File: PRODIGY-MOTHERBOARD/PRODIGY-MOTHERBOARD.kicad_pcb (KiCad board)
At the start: 2 copper layers, 165 x 125 mm, 285 parts, among them J10 RTD_PT100, J11 Can, J12 USB_A, J13 SPI_OUT, J14 MOTOR, J15 12V OUT, J16 Neopixel, J17 SERIAL, J18 I2C, J19 KEYPAD_MATRIX, J2 USB_C_Receptacle, J20 OLED, J21 DM3BT-DSF-PEJS/C, J3 Conn_02x20_Odd_Even, J5 Barrel_Jack_MountingPin, J6 USB_C_Receptacle, J9 A_IN, Q1 BC850, Q2 BC850, Q3 BS870, Q4 BC850, Q5 ALS-PDIC15-21B/TR8, SW1 SW_Push, SW2 SW_Push, SW3 SW_Push, SW4 SW_Push, SW5 SW_Push, SW6 SW_Push, U1 RT9742AGJ5F, U10 PCF8574, U11 HDC1080, U12 LIS2DH12TR, U13 TXS0108EPW, U15 CC56-12YWA, U16 PN5321A3HN_C1xx, U17 CR2013-MI2120, U18 SN74LVC1T45DBV, U19 TSDP341xx, U2 TPS54331DR, U20 TSDP341xx, U21 MCP6021RT-E/OT, U22 LMP2011, U23 LM4125AIM5-2.5, U24 LMP2011, U25 LMP2011, U26 LMP2011, U27 IP4252CZ16, U28 RT9742AGJ5F, U3 TPS54331DR, U4 TJA1051T-E, U5 DRV8870DDA, U6 PCA9306DC, U7 PCA9306DC, U8 SN74LVC1T45DBV, U9 PCF8574

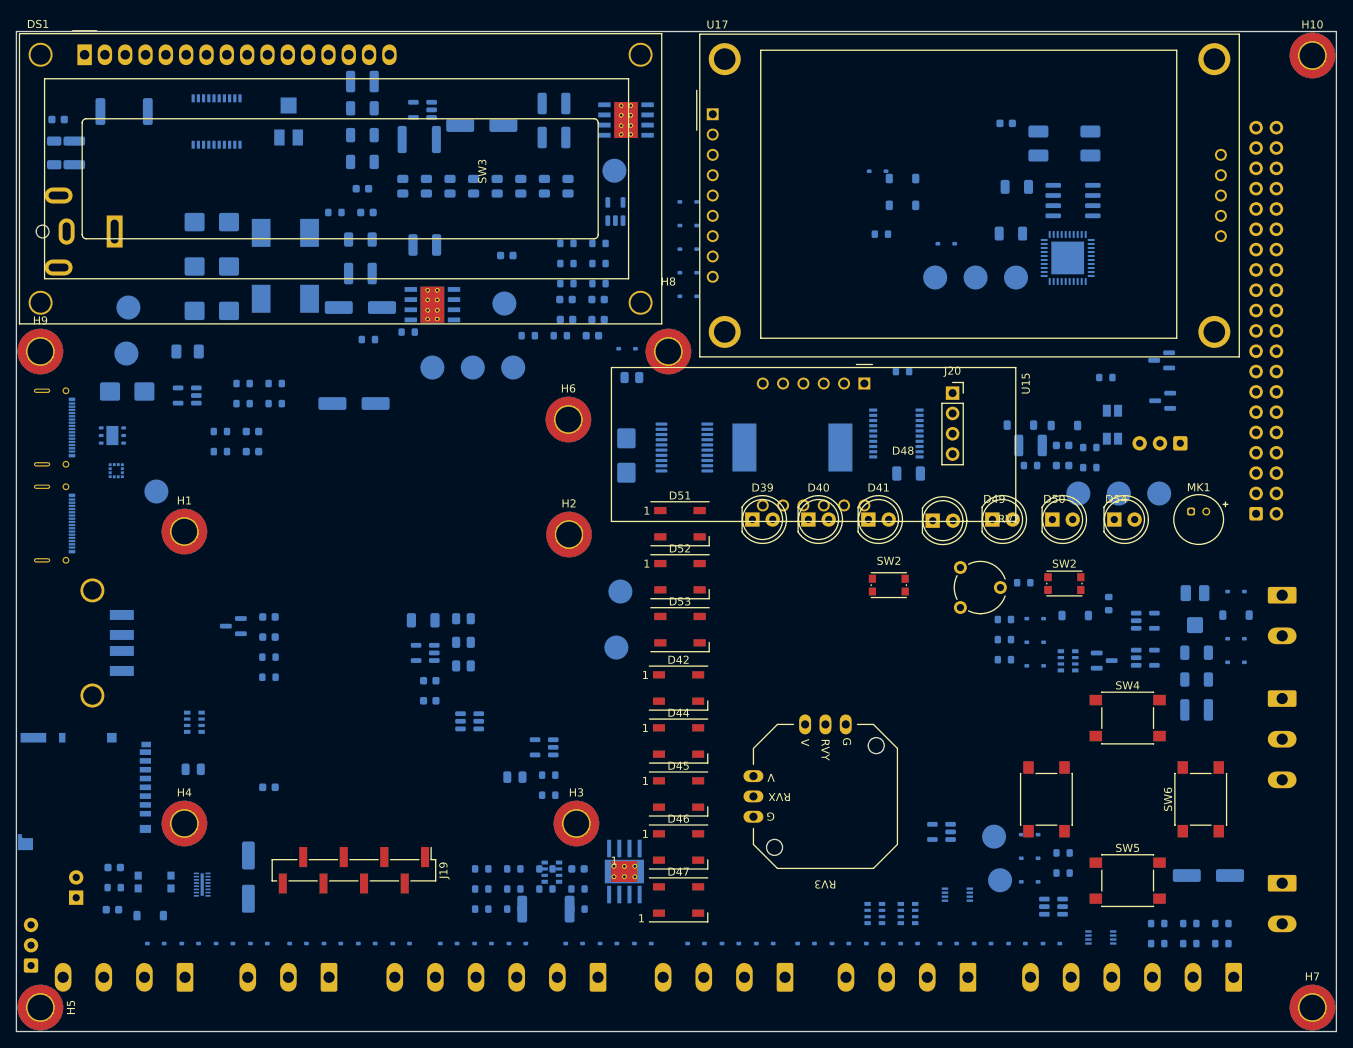
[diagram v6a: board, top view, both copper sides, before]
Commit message: changed breakout connectors and bpc size
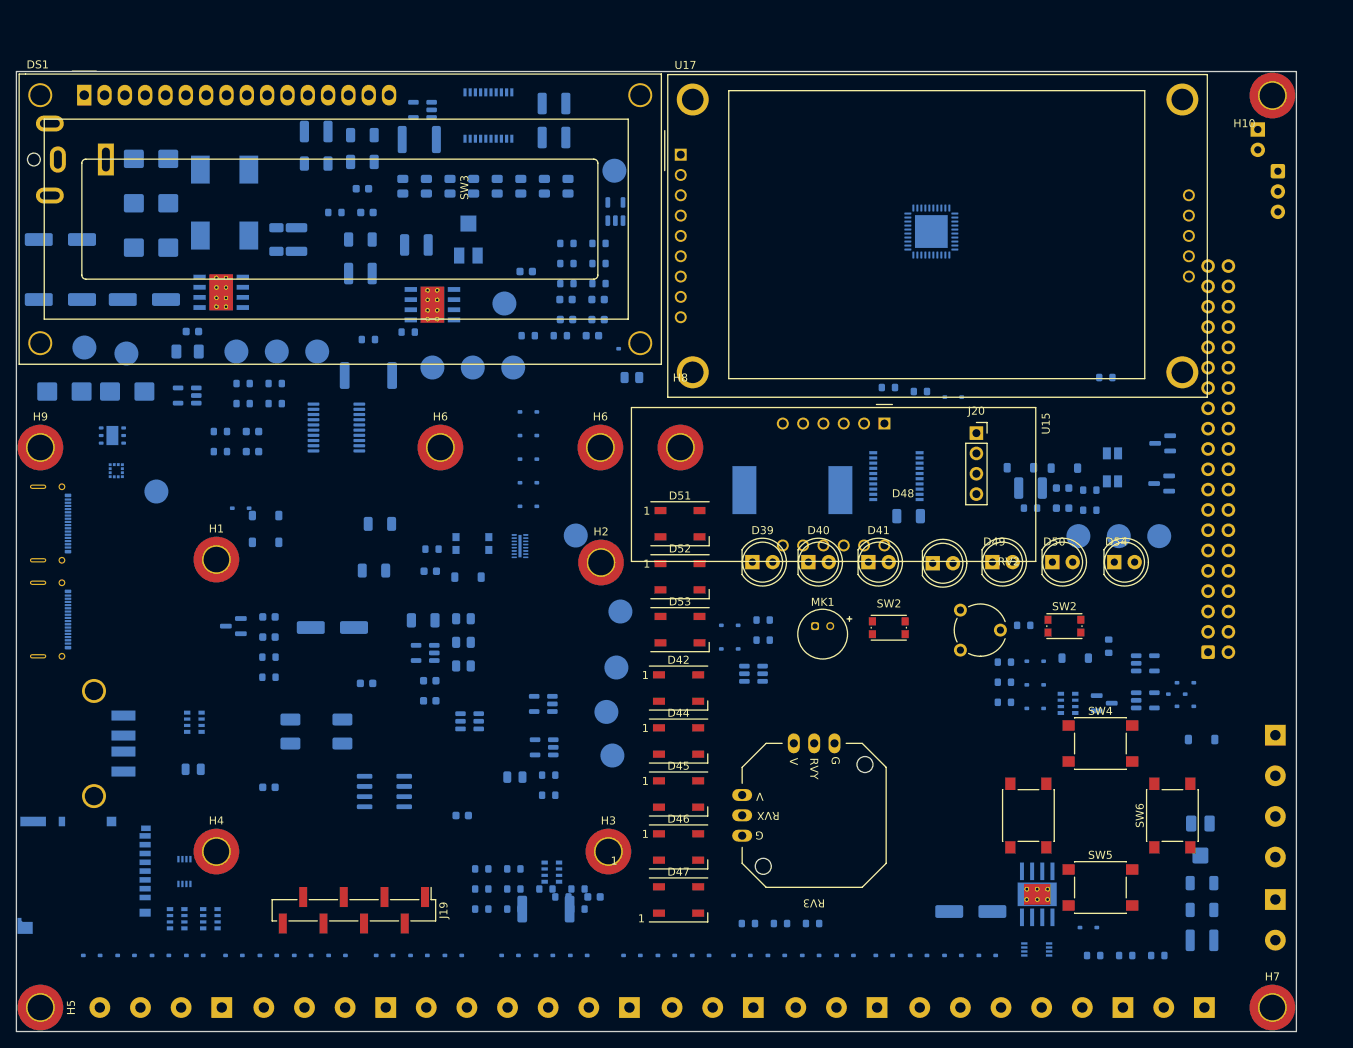
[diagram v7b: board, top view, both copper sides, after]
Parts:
- removed U20: TSDP341xx, OptoDevice:Vishay_MOLD-3Pin
- added H6: MountingHole, MountingHole:MountingHole_3.2mm_M3_ISO7380_Pad_TopBottom, F.Cu at (121.0, 72.0)
- D43: value D_IR_EMITTER -> LL-304PDD2E; footprint LED_THT:LED_D5.0mm_Horizontal_O1.27mm_Z3.0mm_Clear -> LED_THT:LED_D3.0mm_Horizontal_O1.27mm_Z2.0mm_IRBlack
- J10, J17, J18: footprint Connector_Phoenix_MSTB:PhoenixContact_MSTBA_2,5_4-G-5,08_1x04_P5.08mm_Horizontal -> TerminalBlock_Phoenix:TerminalBlock_Phoenix_MKDS-1,5-4-5.08_1x04_P5.08mm_Horizontal
- J11, J16: footprint Connector_Phoenix_MSTB:PhoenixContact_MSTBA_2,5_3-G-5,08_1x03_P5.08mm_Horizontal -> TerminalBlock_Phoenix:TerminalBlock_Phoenix_MKDS-1,5-3-5.08_1x03_P5.08mm_Horizontal
- J13, J14: footprint Connector_Phoenix_MSTB:PhoenixContact_MSTBA_2,5_6-G-5,08_1x06_P5.08mm_Horizontal -> TerminalBlock_Phoenix:TerminalBlock_Phoenix_MKDS-1,5-6-5.08_1x06_P5.08mm_Horizontal
- J15, J9: footprint Connector_Phoenix_MSTB:PhoenixContact_MSTBA_2,5_2-G-5,08_1x02_P5.08mm_Horizontal -> TerminalBlock_Phoenix:TerminalBlock_Phoenix_MKDS-1,5-2-5.08_1x02_P5.08mm_Horizontal
- U19: value TSDP341xx -> OSRB38C9BA
- moved D43 176.2 mm to (223.2, 32.2), turned to -90 degrees
- moved J10 139.6 mm to (225.4, 108.0), turned to -90 degrees
- moved L4 118.9 mm to (105.5, 107.5)
- moved U4 113.4 mm to (114.0, 115.0)
- moved C27 106.3 mm to (111.8, 101.5)
- moved U7 96.7 mm to (89.0, 125.0), turned to -90 degrees
- moved J17 93.3 mm to (93.7, 142.0)
- moved R23 90.1 mm to (113.4, 81.5)
- moved D59 90.1 mm to (99.2, 80.5)
- moved D63 90.1 mm to (99.2, 83.8)
- moved D65 90.1 mm to (96.0, 79.6)
- moved R24 90.1 mm to (112.7, 87.4)
- moved TP3 87.8 mm to (100.5, 60.0)
- moved TP2 87.8 mm to (95.5, 60.0)
- moved TP4 87.8 mm to (105.6, 60.0)
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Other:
- board size 165 x 125 mm -> 160 x 120 mm

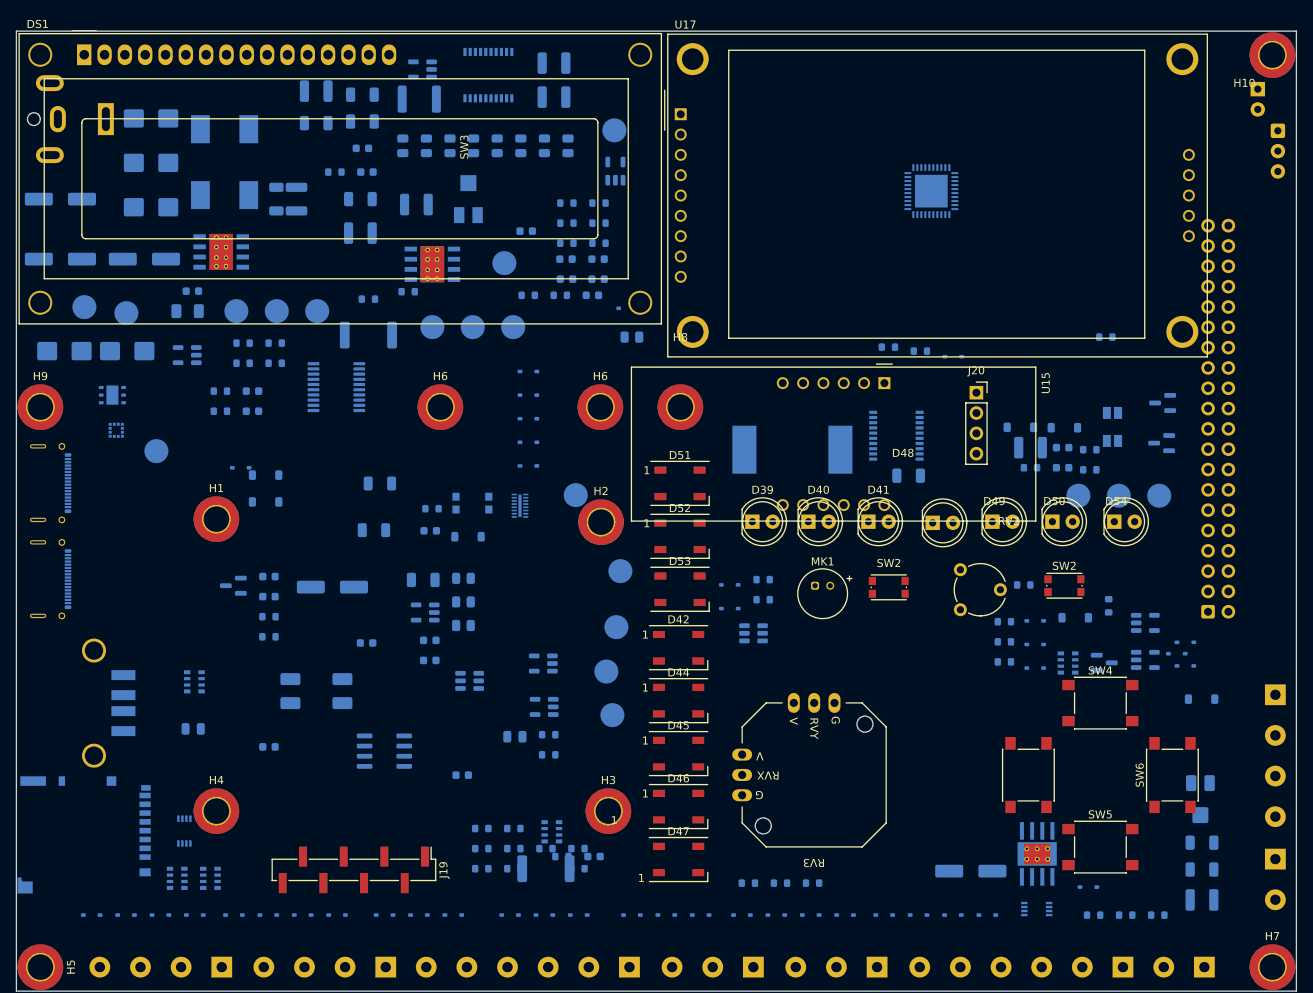
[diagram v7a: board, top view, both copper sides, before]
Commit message: ESP32 schematic complete.
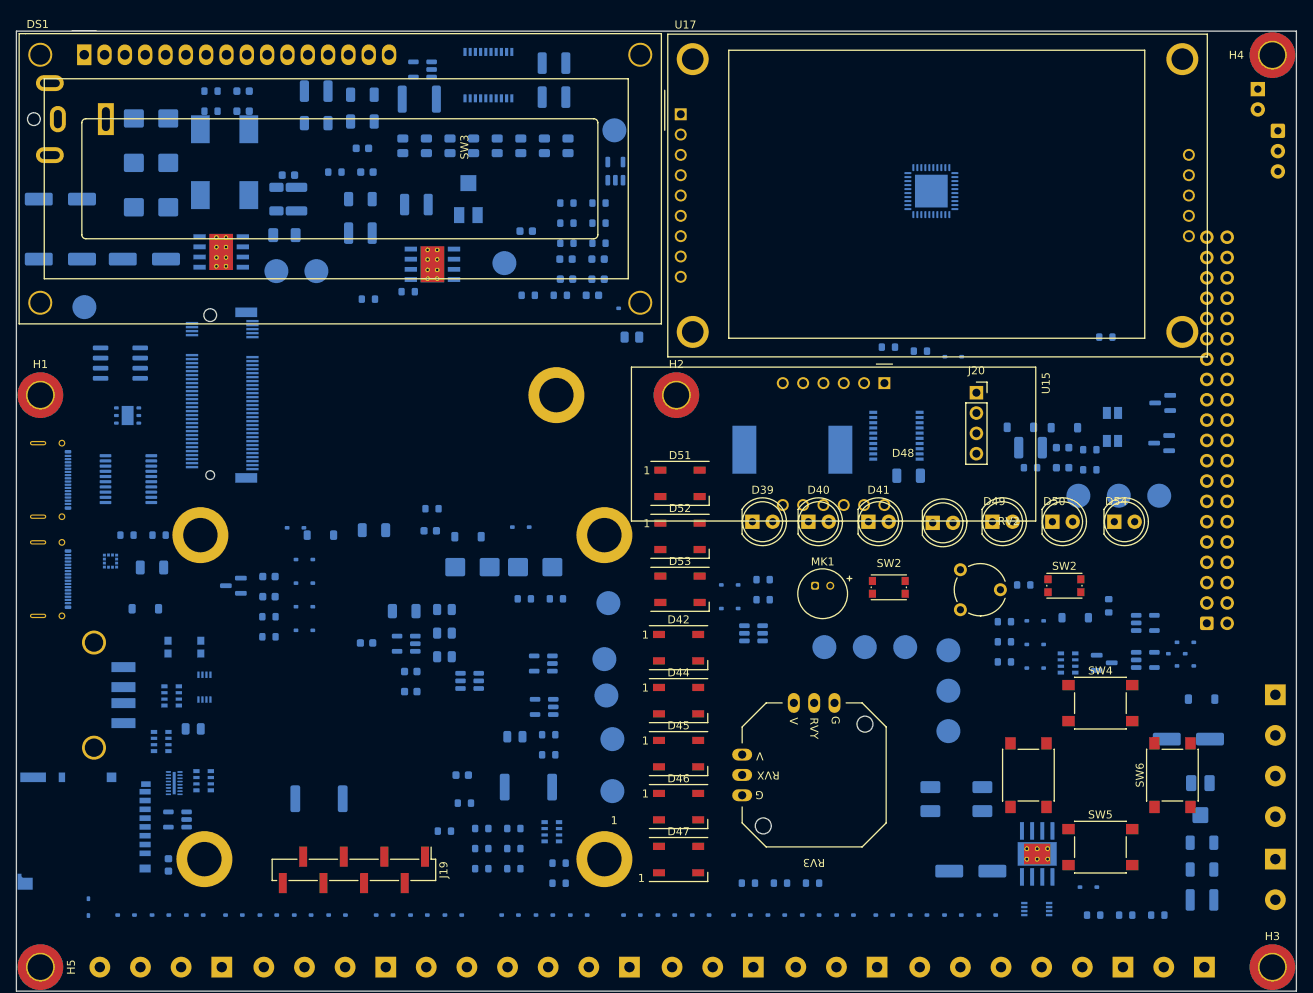
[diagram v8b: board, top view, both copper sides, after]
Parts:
- removed the H6 at (141.0, 72.0)
- added J7: Bus_M.2_Socket_B, m.2_edge_connector_key_a:121992304, B.Cu at (93.6, 70.5)
- H10, H6, H7, H8, H9: footprint MountingHole:MountingHole_3.2mm_M3_ISO7380_Pad_TopBottom -> MountingHole:MountingHole_4.3mm_M4_ISO14580_Pad; moved to B.Cu
- moved H4 162.3 mm to (225.0, 28.0)
- moved C32 108.7 mm to (214.5, 113.5)
- moved TP2 103.3 mm to (184.5, 112.5), turned to 0 degrees
- moved H7 99.4 mm to (141.5, 88.0), turned to 180 degrees
- moved H10 99.1 mm to (135.5, 70.5), turned to 180 degrees
- moved TP3 96.4 mm to (184.5, 107.5), turned to 0 degrees
- moved TP4 89.6 mm to (184.5, 102.4), turned to 0 degrees
- moved H3 85.3 mm to (225.0, 142.0)
- moved L4 81.1 mm to (185.5, 121.0)
- moved TP18 63.3 mm to (174.1, 102.0)
- moved TP17 63.3 mm to (169.0, 102.0)
- moved TP19 63.3 mm to (179.1, 102.0)
- moved H9 60.1 mm to (91.5, 128.5), turned to 180 degrees
- moved U4 58.7 mm to (81.0, 66.5)
- moved R25 58.3 mm to (105.8, 121.0)
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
